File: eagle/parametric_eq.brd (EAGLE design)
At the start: 100 x 80 mm, 42 parts, among them IC1 TL072P, IC2 TL072P

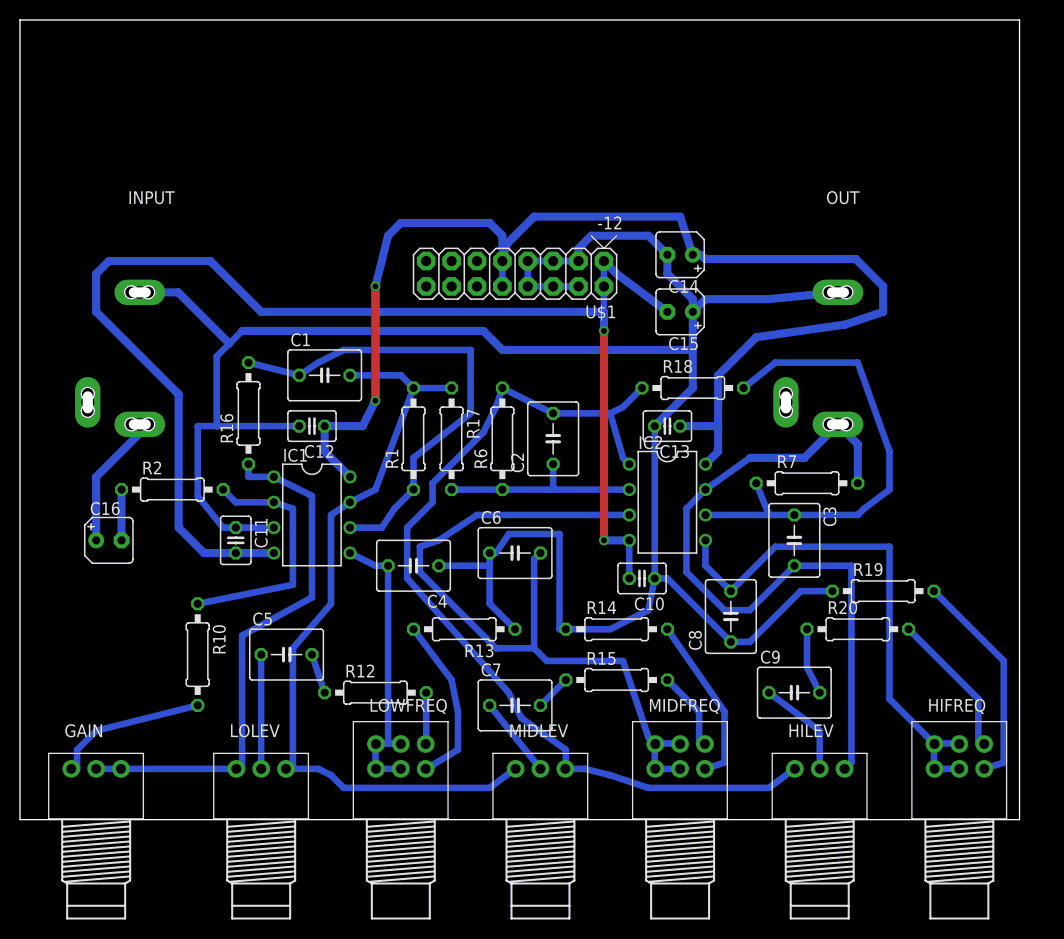
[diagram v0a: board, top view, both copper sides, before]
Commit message: ferrite beads and thick traces
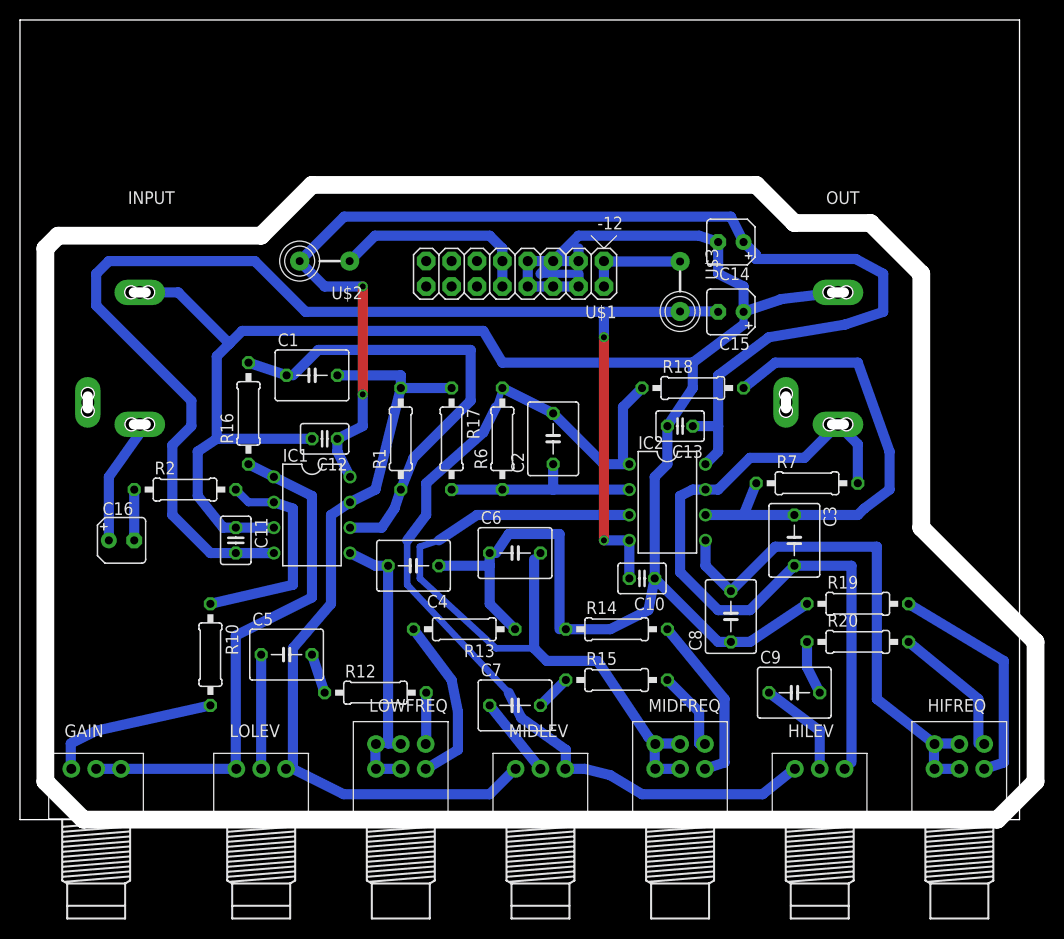
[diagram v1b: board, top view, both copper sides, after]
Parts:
- added U$2, U$3: FB, adafruit:FB
- moved C14 5.24 mm to (71.1, 57.8)
- moved C15 5.08 mm to (71.1, 50.8)
- moved R19 2.84 mm to (83.8, 21.6)
- moved C12 1.80 mm to (30.5, 38.1)
- moved C13 1.27 mm to (66.0, 39.4)
- moved R2 1.27 mm to (16.5, 33.0)
- moved C1 1.27 mm to (29.2, 44.5)
- moved C16 1.27 mm to (10.2, 27.9)
- moved R10 1.27 mm to (19.1, 16.5)
- moved R20 1.27 mm to (83.8, 17.8)
- moved R1 1.27 mm to (38.1, 38.1)
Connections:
- new net N$25: U$1.10, U$1.9, U$2.P$1
- new net N$26: U$1.1, U$1.2, U$3.P$1
- net +12V: now also U$2.P$2; no longer U$1.10, U$1.9
- net -12V: now also U$3.P$2; no longer U$1.1, U$1.2
- net GND: no longer U$1.3, U$1.4, U$1.5, U$1.6, U$1.7, U$1.8
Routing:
- net N$25: track 0.00 -> 20.7 mm
- net GND: track 234.5 -> 245.6 mm
- net N$26: track 0.00 -> 10.2 mm
- net N$7: track 93.0 -> 96.9 mm
- net -12V: track 135.3 -> 138.5 mm
- net N$1: track 24.9 -> 22.4 mm
- net N$8: track 72.0 -> 74.2 mm
- net N$6: track 77.8 -> 79.8 mm
- net N$2: track 15.7 -> 17.1 mm
- net N$20: track 6.65 -> 5.38 mm
- net N$18: track 22.1 -> 23.3 mm
- net N$27: track 74.7 -> 73.5 mm
- net N$23: track 54.1 -> 53.1 mm
- net N$19: track 14.9 -> 14.1 mm
- net N$9: track 13.4 -> 12.6 mm
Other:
- board size 100 x 80 mm -> 101.6 x 80 mm
